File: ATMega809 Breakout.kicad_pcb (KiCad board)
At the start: 2 copper layers, 77.9 x 41.4 mm, 51 parts, among them J1 USB_B_Micro, J2 Conn_01x05, J3 Conn_01x20, J4 Conn_01x12, J5 UPDI, Q1 PJA3438-AU, Q2 PJA3438-AU, Q3 PJA3438-AU, Q4 PJA3438-AU, Q5 PJA3438-AU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

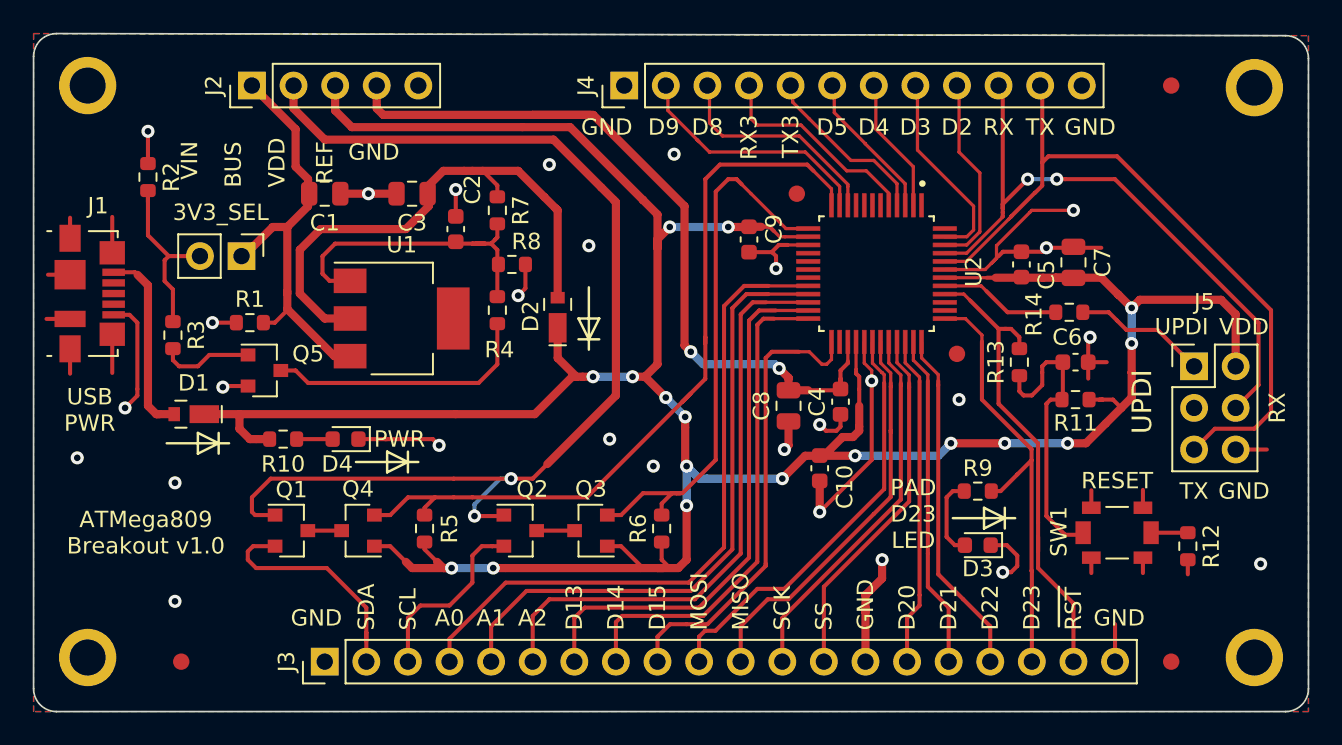
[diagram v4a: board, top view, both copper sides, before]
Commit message: Tweak RST protection resistor placement.
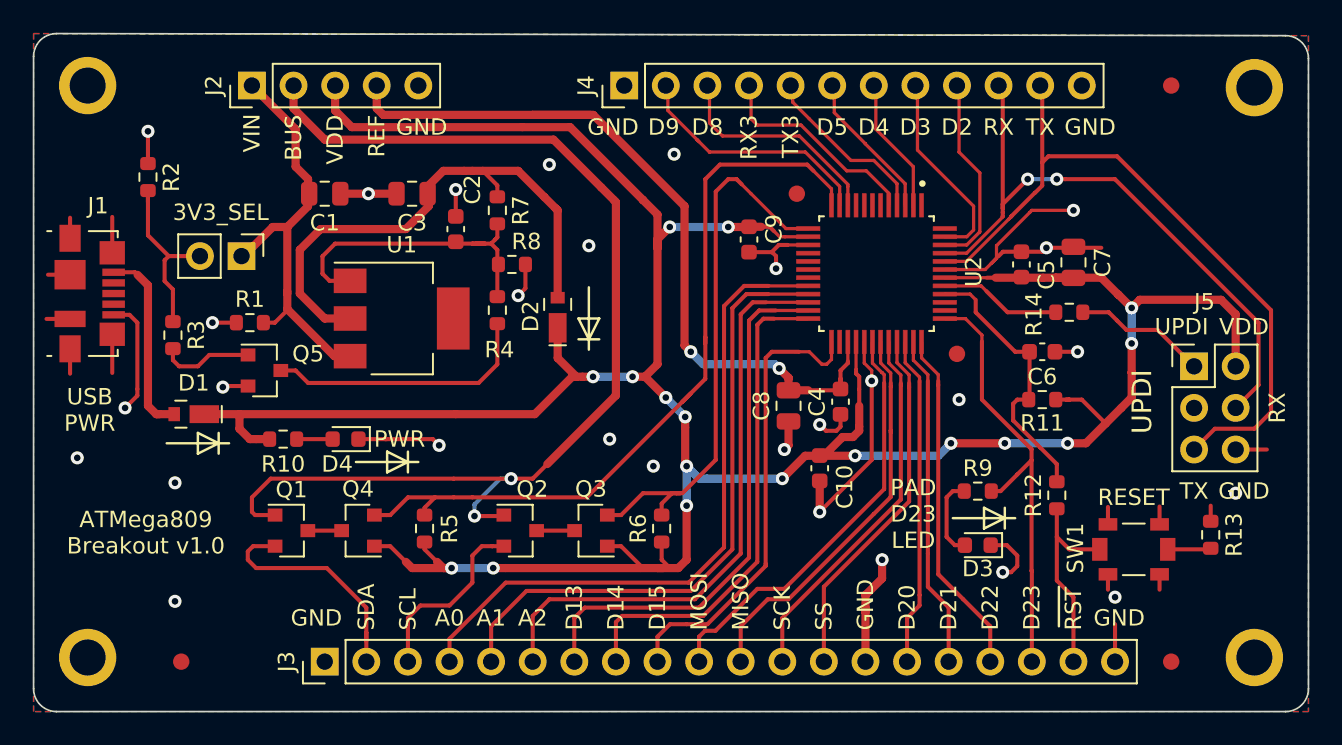
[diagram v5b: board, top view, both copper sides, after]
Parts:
- moved R13 15.7 mm to (172.2, 63.0), turned to 270 degrees
- moved R12 8.58 mm to (162.8, 60.6), turned to 90 degrees
- moved C6 2.13 mm to (161.9, 51.8)
- moved R11 2.03 mm to (161.9, 54.7)
- moved SW1 1.44 mm to (167.5, 63.9)
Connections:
- C6 pad 2: Net-(C6-Pad2) -> /RESET_MCU_L
- J3 pad 19: /RESET_L -> RESET_L
- R11 pad 2: Net-(C6-Pad2) -> /RESET_MCU_L
- R12 pad 1: Net-(R12-Pad1) -> RESET_L
- R12 pad 2: GND -> /RESET_MCU_L
- R13 pad 1: Net-(C6-Pad2) -> GND
- R13 pad 2: /RESET_L -> Net-(R13-Pad2)
- SW1 pad 1: Net-(C6-Pad2) -> RESET_L
- SW1 pad 2: Net-(R12-Pad1) -> Net-(R13-Pad2)
- U2 pad 40: /RESET_L -> /RESET_MCU_L
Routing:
- net /RESET_L: track 29.0 -> 0.00 mm
- net Net-(C6-Pad2): track 18.3 -> 0.00 mm
- net /RESET_MCU_L: track 0.00 -> 17.1 mm
- net RESET_L: track 0.00 -> 12.1 mm
- net GND: track 98.4 -> 95.8 mm, vias 28 -> 29
- net Net-(R13-Pad2): track 0.00 -> 2.62 mm
- net Net-(R12-Pad1): track 2.37 -> 0.00 mm
- net VDD: track 188.3 -> 189.8 mm

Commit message: Final tweaks and checks.
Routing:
- net GND: track 95.8 -> 97.3 mm
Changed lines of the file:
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@@
     (thickness 1.6)
     (drawings 89)
-    (tracks 680)
+    (tracks 682)
     (zones 0)
     (modules 51)
@@
   (segment (start 105.134 45.7725) (end 105.134 43.583) (width 0.25) (layer F.Cu) (net 1))
   (segment (start 102.559 44.885) (end 102.559 43.631) (width 0.25) (layer F.Cu) (net 1))
-  (segment (start 102.559 47.11) (end 101.212 47.11) (width 0.25) (layer F.Cu) (net 1))
-  (segment (start 102.559 49.81) (end 101.118 49.81) (width 0.25) (layer F.Cu) (net 1))
   (via (at 135.509 57.15) (size 0.8) (drill 0.4) (layers F.Cu B.Cu) (net 1))
   (segment (start 129.921 48.387) (end 130.365 47.943) (width 0.25) (layer F.Cu) (net 1))
@@
   (via (at 173.736 60.452) (size 0.8) (drill 0.4) (layers F.Cu B.Cu) (net 1))
   (via (at 166.37 66.802) (size 0.8) (drill 0.4) (layers F.Cu B.Cu) (net 1))
+  (segment (start 102.559 51.635) (end 102.559 49.968) (width 0.25) (layer F.Cu) (net 1))
+  (segment (start 102.559 47.11) (end 102.496 47.11) (width 0.25) (layer F.Cu) (net 1))
+  (segment (start 102.496 47.11) (end 102.616 46.99) (width 0.25) (layer F.Cu) (net 1))
+  (segment (start 102.616 46.99) (end 102.616 44.577) (width 0.25) (layer F.Cu) (net 1))
   (segment (start 118.696 52.084) (end 115.824 49.212) (width 0.5) (layer F.Cu) (net 2))
   (segment (start 119.659 52.084) (end 118.696 52.084) (width 0.5) (layer F.Cu) (net 2))

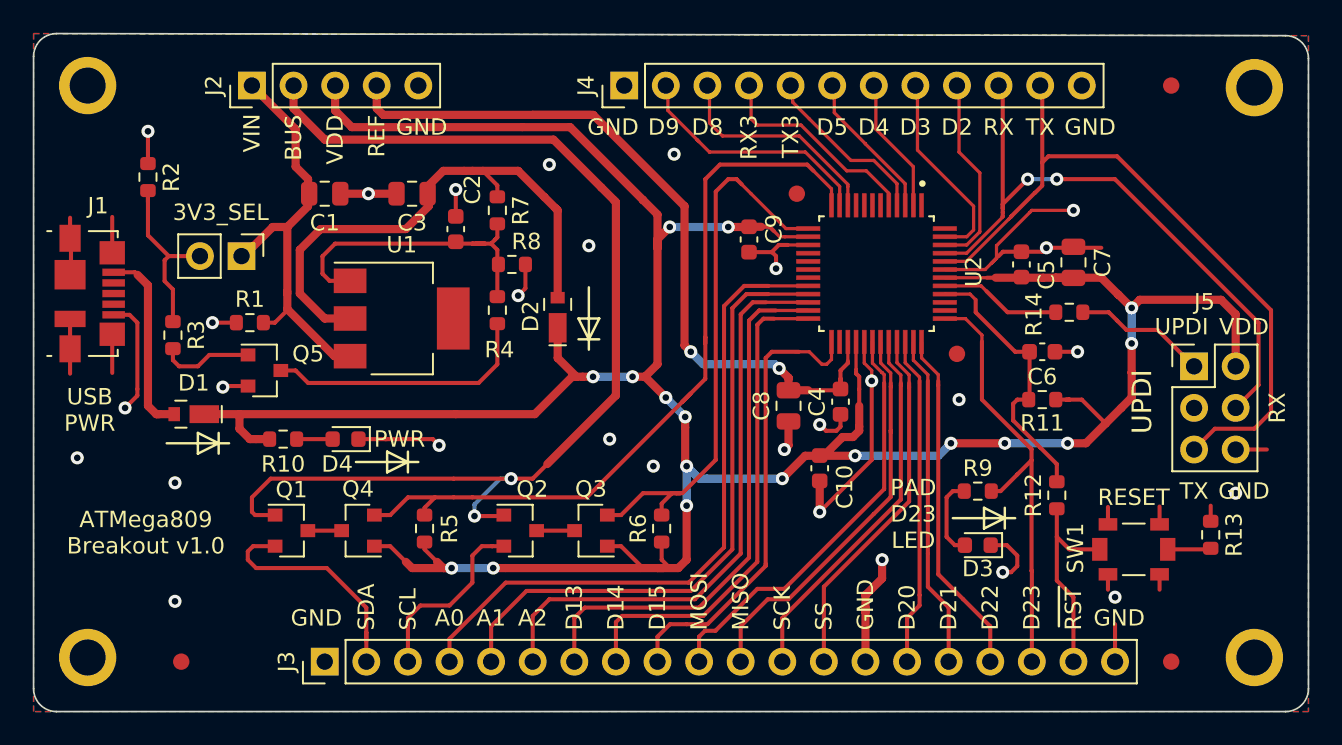
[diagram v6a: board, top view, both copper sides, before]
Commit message: v1.0 Release to manufacturing
* Add BOM data to KiCAD and export to Excel.
* Elaborate on fab notes TXT file.
* Generate gerber files, schematic pdf, drill file, placement file for mfr.
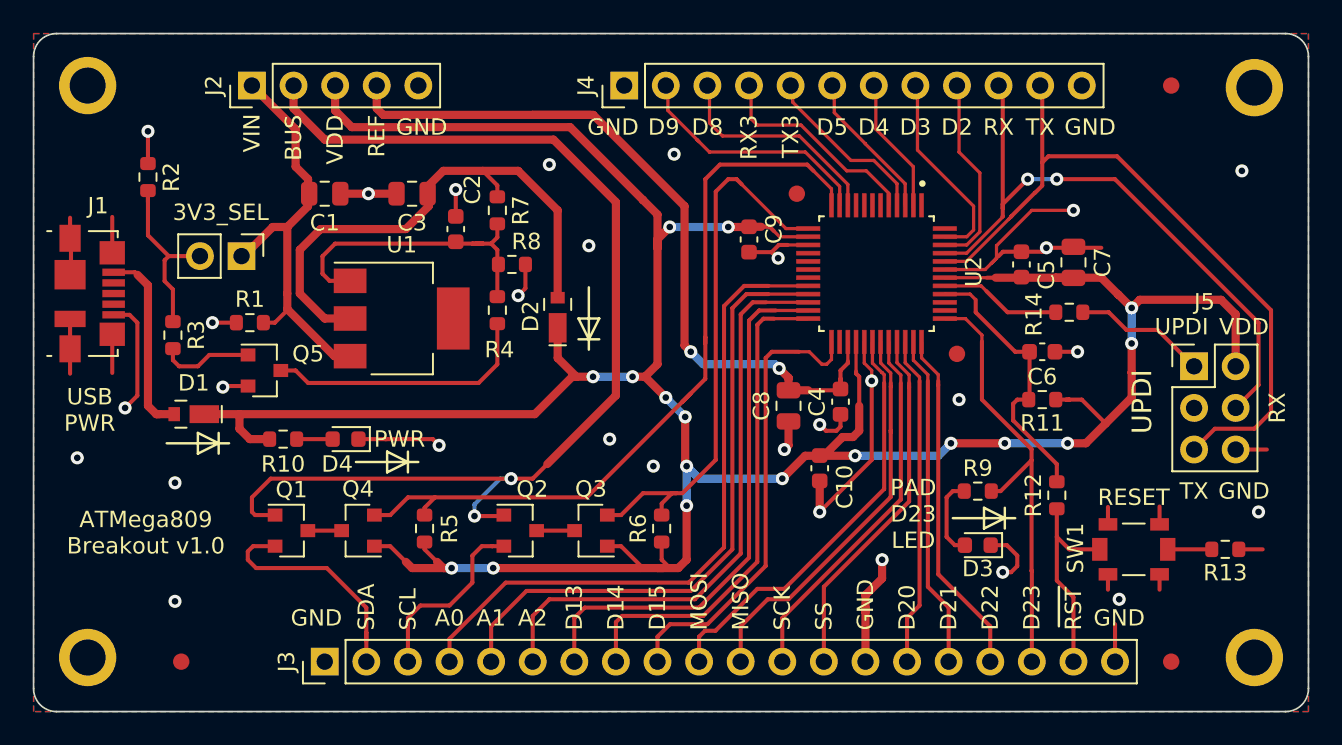
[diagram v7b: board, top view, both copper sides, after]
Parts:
- moved R13 1.26 mm to (173.1, 63.9), turned to 180 degrees
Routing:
- net /SCL_MCU: track 34.2 -> 33.7 mm
- net GND: vias 29 -> 30
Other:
- outline, holes or cut-outs redrawn

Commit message: Upgrade to KiCAD 6.0 format.
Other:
- net class Default removed
- net class POWER removed
